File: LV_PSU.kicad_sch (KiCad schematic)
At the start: 25 parts, among them IC201 1769205241, J201 Header_Male_Pin_2.54mm_1X2_,_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, J202 PJ-082BH, U201 OKI-78SR-5_1.5-W36H-C, U202 AZ1117IH-3.3TRG1, U203 AZ1117IH-3.3TRG1

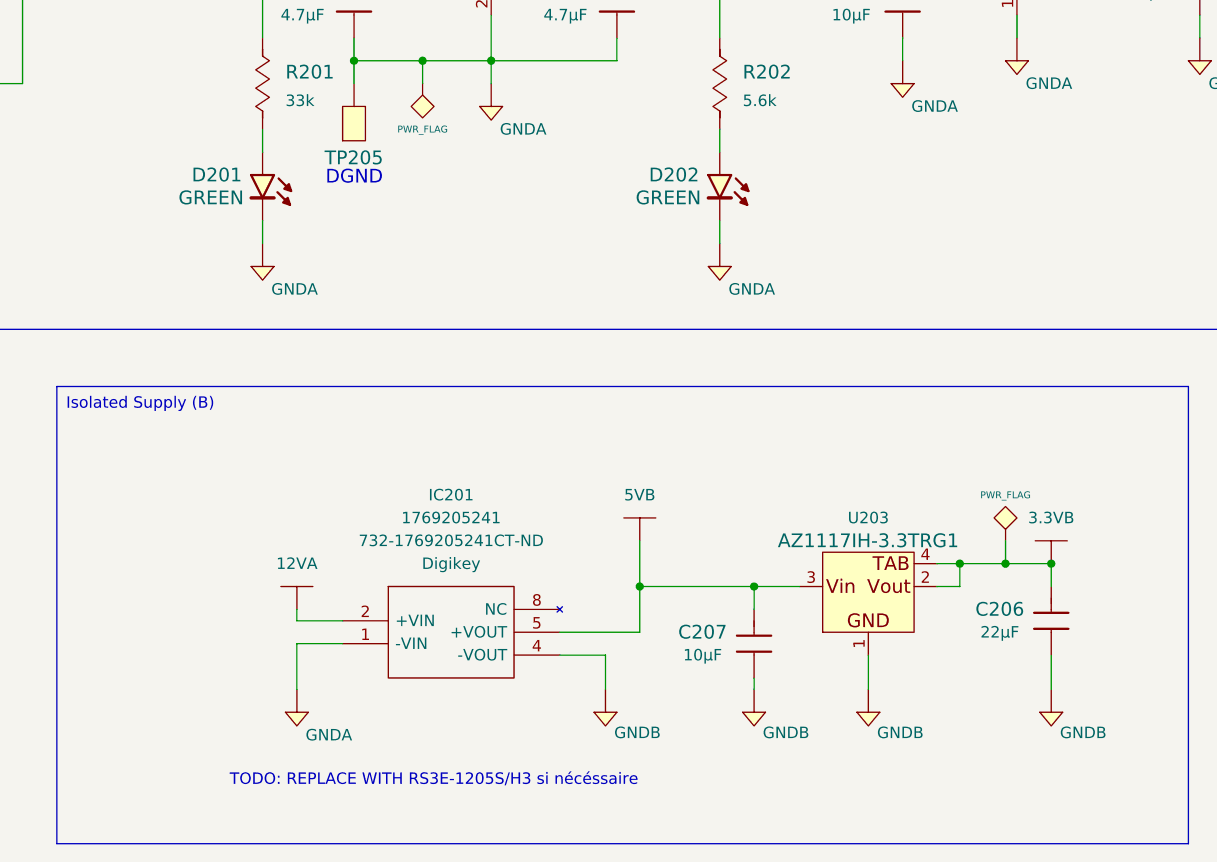
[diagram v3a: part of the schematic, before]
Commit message: update schematic
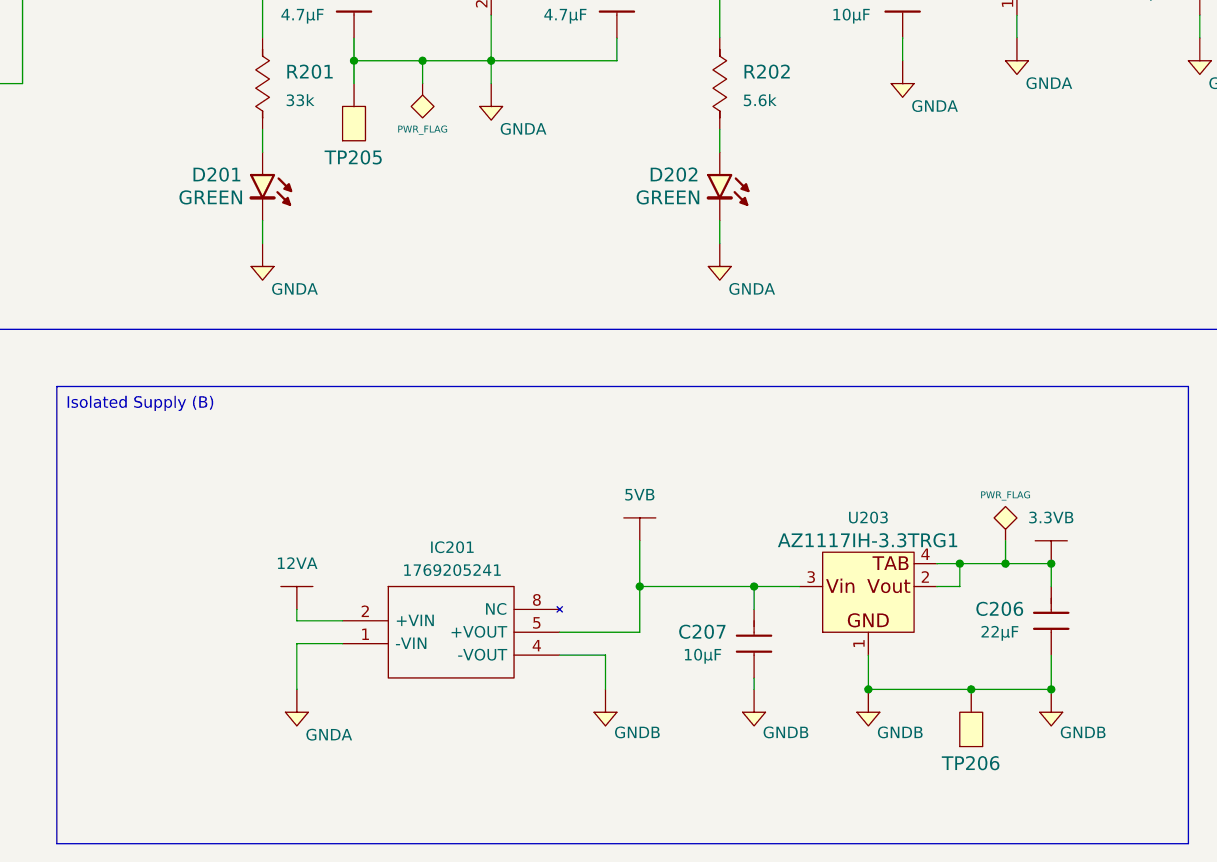
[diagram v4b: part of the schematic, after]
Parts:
- added TP206: Test_Point_THM, Connectors:Keystone_5001, symbol Connectors:Test_Point_THM
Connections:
- net GNDB: now also TP206.1 (TP)
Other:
- note removed: "DGND"
- note removed: "TODO: REPLACE WITH RS3E-1205S/H3 si nécéssaire"
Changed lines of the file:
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@@
 	)
 	(junction
+		(at 186.69 140.97)
+		(diameter 0)
+		(color 0 0 0 0)
+	)
+	(junction
 		(at 85.09 58.42)
 		(diameter 0)
@@
 	)
 	(junction
+		(at 175.26 140.97)
+		(diameter 0)
+		(color 0 0 0 0)
+	)
+	(junction
 		(at 118.11 71.12)
 		(diameter 0)
@@
 	)
 	(junction
+		(at 195.58 140.97)
+		(diameter 0)
+		(color 0 0 0 0)
+	)
+	(junction
 		(at 171.45 58.42)
 		(diameter 0)
@@
 	(wire
 		(pts
+			(xy 175.26 140.97) (xy 186.69 140.97)
+		)
+		(stroke
+			(width 0)
+			(type default)
+		)
+	)
+	(wire
+		(pts
 			(xy 185.42 127) (xy 185.42 129.54)
 		)
@@
 	(wire
 		(pts
+			(xy 186.69 140.97) (xy 195.58 140.97)
+		)
+		(stroke
+			(width 0)
+			(type default)
+		)
+	)
+	(wire
+		(pts
 			(xy 179.07 60.96) (xy 179.07 58.42)
 		)
@@
 		)
 	)
-	(text "TODO: REPLACE WITH RS3E-1205S/H3 si nécéssaire"
-		(exclude_from_sim no)
-		(at 127 151.13 0)
-		(effects
-			(font
-				(size 1.27 1.27)
-			)
-		)
-	)
 	(text "12V IN"
 		(exclude_from_sim no)
@@
 		)
 	)
-	(text "DGND"
-		(exclude_from_sim no)
-		(at 114.935 85.09 0)
-		(effects
-			(font
-				(size 1.524 1.524)
-			)
-			(justify left bottom)
-		)
-	)
 	(symbol
 		(lib_id "Connectors:PJ-082BH")
@@
 		(on_board yes)
 		(dnp no)
-		(fields_autoplaced yes)
 		(property "Reference" "IC201"
-			(at 128.905 119.38 0)
+			(at 129.032 125.222 0)
 			(effects
 				(font
@@
 		)
 		(property "Value" "1769205241"
-			(at 128.905 121.92 0)
+			(at 129.032 127.762 0)
 			(effects
 				(font
@@
 					(size 1.27 1.27)
 				)
+				(hide yes)
 			)
 		)
@@
 					(size 1.27 1.27)
 				)
+				(hide yes)
 			)
 		)
@@
 	)
 	(symbol
+		(lib_id "Connectors:Test_Point_THM")
+		(at 186.69 146.05 90)
+		(unit 1)
+		(exclude_from_sim no)
+		(in_bom yes)
+		(on_board yes)
+		(dnp no)
+		(property "Reference" "TP206"
+			(at 186.69 149.225 90)
+			(effects
+				(font
+					(size 1.524 1.524)
+				)
+			)
+		)
+		(property "Value" "Test_Point_THM"
+			(at 194.31 146.05 0)
+			(effects
+				(font
+					(size 1.524 1.524)
+				)
+				(hide yes)
+			)
+		)
+		(property "Footprint" "Connectors:Keystone_5001"
+			(at 209.55 146.05 0)
+			(effects
+				(font
+					(size 1.524 1.524)
+				)
+				(hide yes)
+			)
+		)
+		(property "Datasheet" "http://keyelco.com/userAssets/file/M65p56.pdf"
+			(at 212.09 146.05 0)
+			(effects
+				(font
+					(size 1.524 1.524)
+				)
+				(hide yes)
+			)
+		)
+		(property "Description" "TEST POINT PC MINI .040\"D BLACK"
+			(at 207.01 146.05 0)
+			(effects
+				(font
+					(size 1.524 1.524)
+				)
+				(hide yes)
+			)
+		)
+		(property "Supplier" "Digikey"
+			(at 196.85 146.05 0)
+			(effects
+				(font
+					(size 1.524 1.524)
+				)
+				(hide yes)
+			)
+		)
+		(property "Supplier Part Number" "36-5001-ND"
+			(at 199.39 146.05 0)
+			(effects
+				(font
+					(size 1.524 1.524)
+				)
+				(hide yes)
+			)
+		)
+		(property "Manufacturer" "Keystone Electronics"
+			(at 201.93 146.05 0)
+			(effects
+				(font
+					(size 1.524 1.524)
+				)
+				(hide yes)
+			)
+		)
+		(property "Manufacturer Part Number" "5001"
+			(at 204.47 146.05 0)
+			(effects
+				(font
+					(size 1.524 1.524)
+				)
+				(hide yes)
+			)
+		)
+		(pin "1"
+		)
+		(instances
+			(project "SACE-HW"
+				(path "/4c1e5ca8-aa0f-4a8e-bffe-6765adb2e3e8/0f8b1d52-3451-4d91-9a0f-fc5eea3d9449"
+					(reference "TP206")
+					(unit 1)
+				)
+			)
+		)
+	)
+	(symbol
 		(lib_id "Capacitors:885012107005")
 		(at 195.58 132.08 90)
@@
 		(on_board yes)
 		(dnp no)
-		(property "Reference" "#PWR0218"
+		(property "Reference" "#PWR0219"
 			(at 175.26 147.828 0)
 			(effects
@@
 			(project "SACE-HW"
 				(path "/4c1e5ca8-aa0f-4a8e-bffe-6765adb2e3e8/0f8b1d52-3451-4d91-9a0f-fc5eea3d9449"
-					(reference "#PWR0218")
+					(reference "#PWR0219")
 					(unit 1)
 				)
@@
 		(on_board yes)
 		(dnp no)
-		(property "Reference" "#PWR0219"
+		(property "Reference" "#PWR0220"
 			(at 195.58 147.828 0)
 			(effects
@@
 			(project "SACE-HW"
 				(path "/4c1e5ca8-aa0f-4a8e-bffe-6765adb2e3e8/0f8b1d52-3451-4d91-9a0f-fc5eea3d9449"
-					(reference "#PWR0219")
+					(reference "#PWR0220")
 					(unit 1)
 				)
@@
 		(on_board yes)
 		(dnp no)
-		(property "Reference" "#PWR0220"
+		(property "Reference" "#PWR0218"
 			(at 162.56 147.828 0)
 			(effects
@@
 			(project "SACE-HW"
 				(path "/4c1e5ca8-aa0f-4a8e-bffe-6765adb2e3e8/0f8b1d52-3451-4d91-9a0f-fc5eea3d9449"
-					(reference "#PWR0220")
+					(reference "#PWR0218")
 					(unit 1)
 				)

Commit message: modif schématique
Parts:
- removed C205, C207: 885012107014, Capacitors:C0805, symbol Capacitors:885012107014
- removed C206: 885012107005, Capacitors:C0805, symbol Capacitors:885012107005
- removed IC201: 1769205241, IC:1769205241, symbol PMIC:1769205241
- removed J201: Header_Male_Pin_2.54mm_1X2_,_Unshrouded, Connectors:Headers_2.54mm_1X2, symbol Connectors:Header_Male_Pin_2.54mm_1X2_,_Unshrouded
- removed J202: PJ-082BH, Connectors:CUI_PJ-082BH, symbol Connectors:PJ-082BH
- removed TP202: Test_Point_THM, Connectors:Keystone_5001, symbol Connectors:Test_Point_THM
- removed U203: AZ1117IH-3.3TRG1, IC:SOT-223-3, symbol PMIC:AZ1117IH-3.3TRG1
- added C205: 885012107005, Capacitors:C0805, symbol Capacitors:885012107005
- added C206, C207: 885012107018, Capacitors:C0805, symbol Capacitors:885012107018
- added C208: 885012107014, Capacitors:C0805, symbol Capacitors:885012107014
- added D204, D205, D206: 150080VS75000, Diodes:LED_0805_GREEN, symbol Diodes:150080VS75000
- added F202: 39511000440, Fuses:TE5_395, symbol Fuses:39511000440
- added J201, J203: 1935161, Connectors:1935161, symbol Connectors:1935161
- added J202: Header_Male_Pin_2.54mm_1X2_,_Unshrouded, Connectors:Headers_2.54mm_1X2, symbol Connectors:Header_Male_Pin_2.54mm_1X2_,_Unshrouded
- added R204: RC0805JR-0733KL, Resistors:R0805, symbol Resistors:RC0805JR-0733KL
- added R205: RC0805FR-075K6L, Resistors:R0805, symbol Resistors:RC0805FR-075K6L
- added R206: RC0805JR-072K2L, Resistors:R0805, symbol Resistors:RC0805JR-072K2L
- added TP205, TP207, TP208, TP209: Test_Point_THM, Connectors:Keystone_5001, symbol Connectors:Test_Point_THM
- added U203: OKI-78SR-5_1.5-W36H-C, Assembly:OKI-78SR_Horizontal, symbol PMIC:OKI-78SR-5_1.5-W36H-C
- added U204: AZ1117IH-3.3TRG1, IC:SOT-223-3, symbol PMIC:AZ1117IH-3.3TRG1
- renumbered TP203 to TP202, TP204 to TP203, TP205 to TP204
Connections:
- net 12VA: now also J201.2
- net 3.3VB: now also C205.2, J202.1, R206.2, TP205.1 (TP), U204.2 (Vout), U204.4 (Vout_(TAB))
- net 5VB: now also C207.2, C208.2, R205.2, TP208.1 (TP), U203.3 (Vout), U204.3 (Vin)
- net GNDA: now also J201.1
- net GNDB: now also C205.1, C206.1, C207.1, C208.1, D204.1 (Cathode), D205.1 (Cathode), D206.1 (Cathode), J203.1, TP209.1 (TP), U203.2 (GND), U204.1 (GND); no longer TP206.1 (TP)
- net VDD: now also TP206.1 (TP), J202.2
- new net: D205.2 (Anode), R205.1
- new net: C206.2, F202.2, R204.2, TP207.1 (TP), U203.1 (Vin)
- new net: D206.2 (Anode), R206.1
- new net: D204.2 (Anode), R204.1
- new net 12VB: F202.1, J203.2
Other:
- note removed: "3.3V (LDO)"
- note removed: "5V (SMPS)"
- moved on the sheet: C201, C202, C203, C204, D201, D202, D203, F201, R201, R202, R203, TP201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

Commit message: update schematique
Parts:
- renumbered C202 to C1, C206 to C2, C203 to C3, C207 to C4, C204 to C5, C208 to C6, C201 to C7, C205 to C8, D201 to D1, D204 to D2, D202 to D3, D205 to D4, D203 to D5, D206 to D6, F201 to F1, F202 to F2, J201 to J1, J203 to J2, J202 to J3, R201 to R1, R204 to R2, R202 to R3, R205 to R4, R203 to R5, R206 to R6, TP202 to TP1, TP207 to TP2, TP204 to TP3, TP209 to TP4, TP203 to TP5, TP208 to TP6, TP201 to TP7, TP205 to TP8, TP206 to TP9, U201 to U1, U203 to U2, U202 to U3, U204 to U4

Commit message: update schematique
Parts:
- removed C1, C3: 885012107018, Capacitors:C0805, symbol Capacitors:885012107018
- removed D1: 150080VS75000, Diodes:LED_0805_GREEN, symbol Diodes:150080VS75000
- removed F1: 39511000440, Fuses:TE5_395, symbol Fuses:39511000440
- removed J1: 1935161, Connectors:1935161, symbol Connectors:1935161
- removed R1: RC0805JR-0733KL, Resistors:R0805, symbol Resistors:RC0805JR-0733KL
- removed TP1, TP3: Test_Point_THM, Connectors:Keystone_5001, symbol Connectors:Test_Point_THM
- removed U1: OKI-78SR-5_1.5-W36H-C, Assembly:OKI-78SR_Horizontal, symbol PMIC:OKI-78SR-5_1.5-W36H-C
- added IC201: 1769205241, IC:1769205241, symbol PMIC:1769205241
- added J203: 2350514-8, Connectors:CONN8_2350514-8_TEC, symbol Connectors:2350514-8
- renumbered C7 to C201, C5 to C202, C8 to C203, C2 to C204, C4 to C205, C6 to C206, D3 to D201, D5 to D202, D2 to D203, D4 to D204, D6 to D205, F2 to F201, J3 to J201, J2 to J202, R3 to R201, R5 to R202, R2 to R203, R4 to R204, R6 to R205, TP7 to TP201, TP5 to TP202, TP8 to TP203, TP9 to TP204, TP2 to TP205, TP6 to TP206, TP4 to TP207, U3 to U201, U2 to U202, U4 to U203
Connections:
- net 12VB: now also IC201.2 (+VIN), J203.1, J203.2
- net 5VA: now also IC201.5 (+VOUT)
- net 5VB: now also J203.3, J203.4
- net GNDA: now also IC201.4 (-VOUT)
- net GNDB: now also IC201.1 (-VIN), J203.5, J203.6, J203.7, J203.8
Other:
- moved on the sheet: C201, C202, C203, C204, C205, C206, D201, D202, D203, D204, D205, F201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

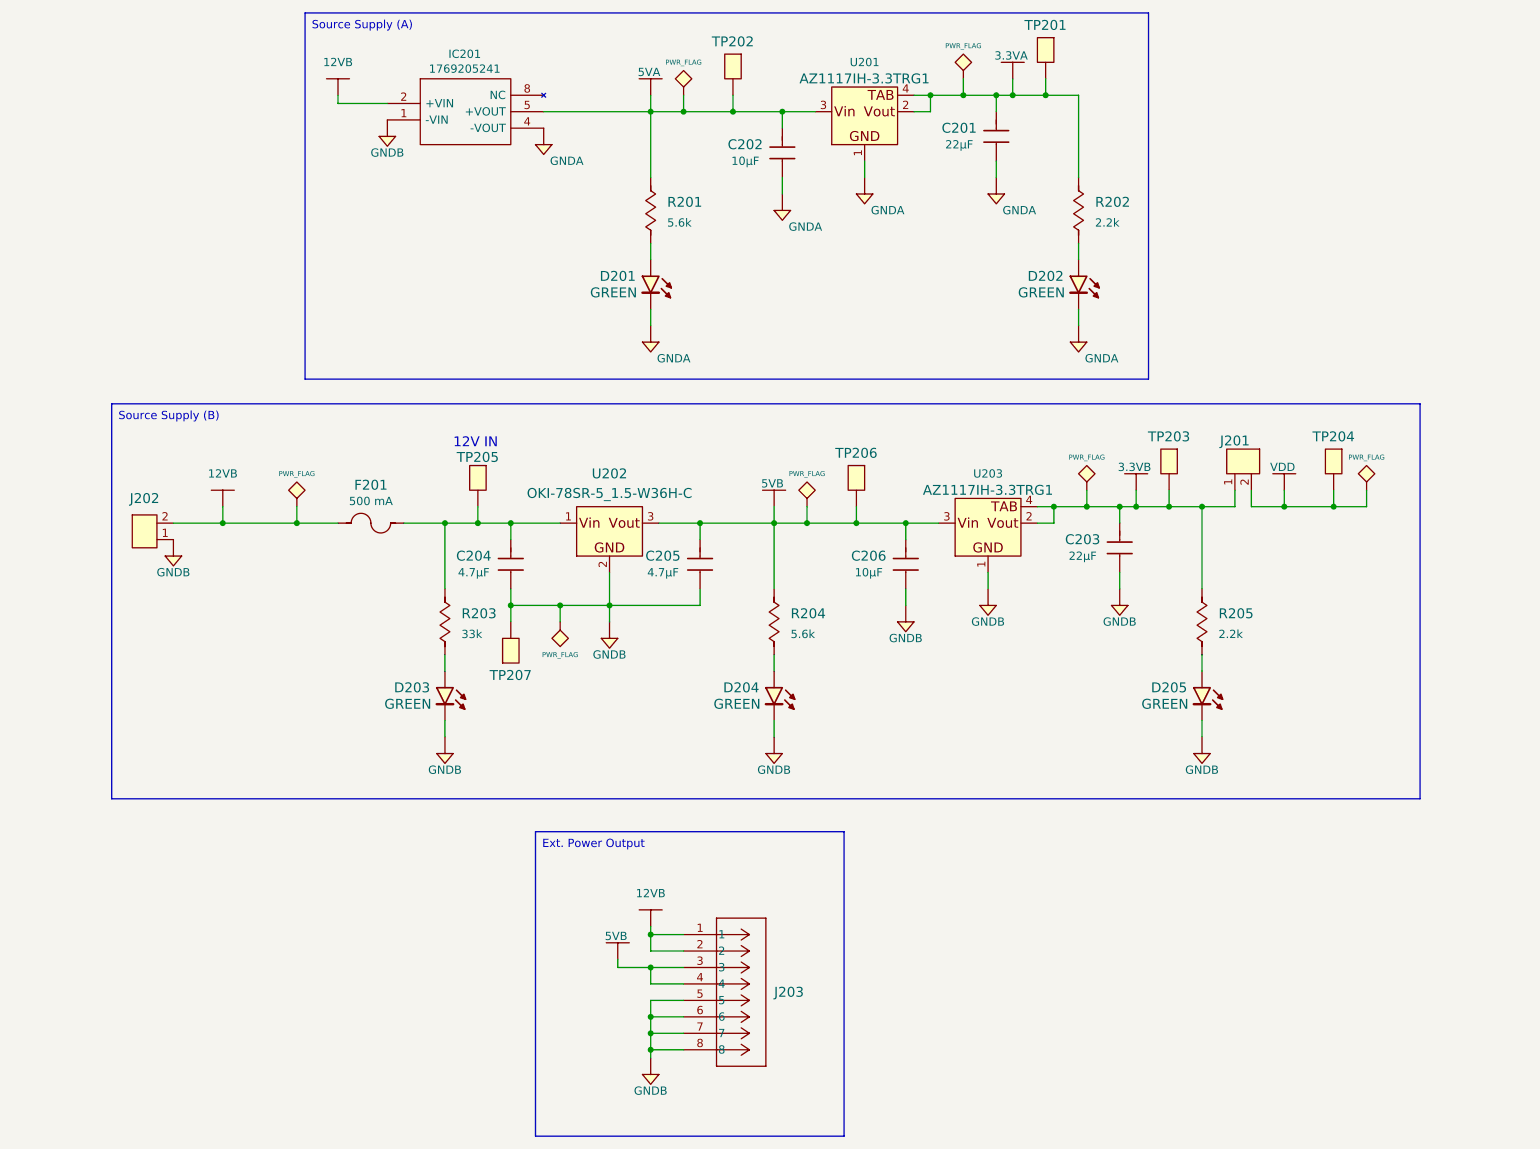
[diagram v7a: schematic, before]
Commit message: update schematic
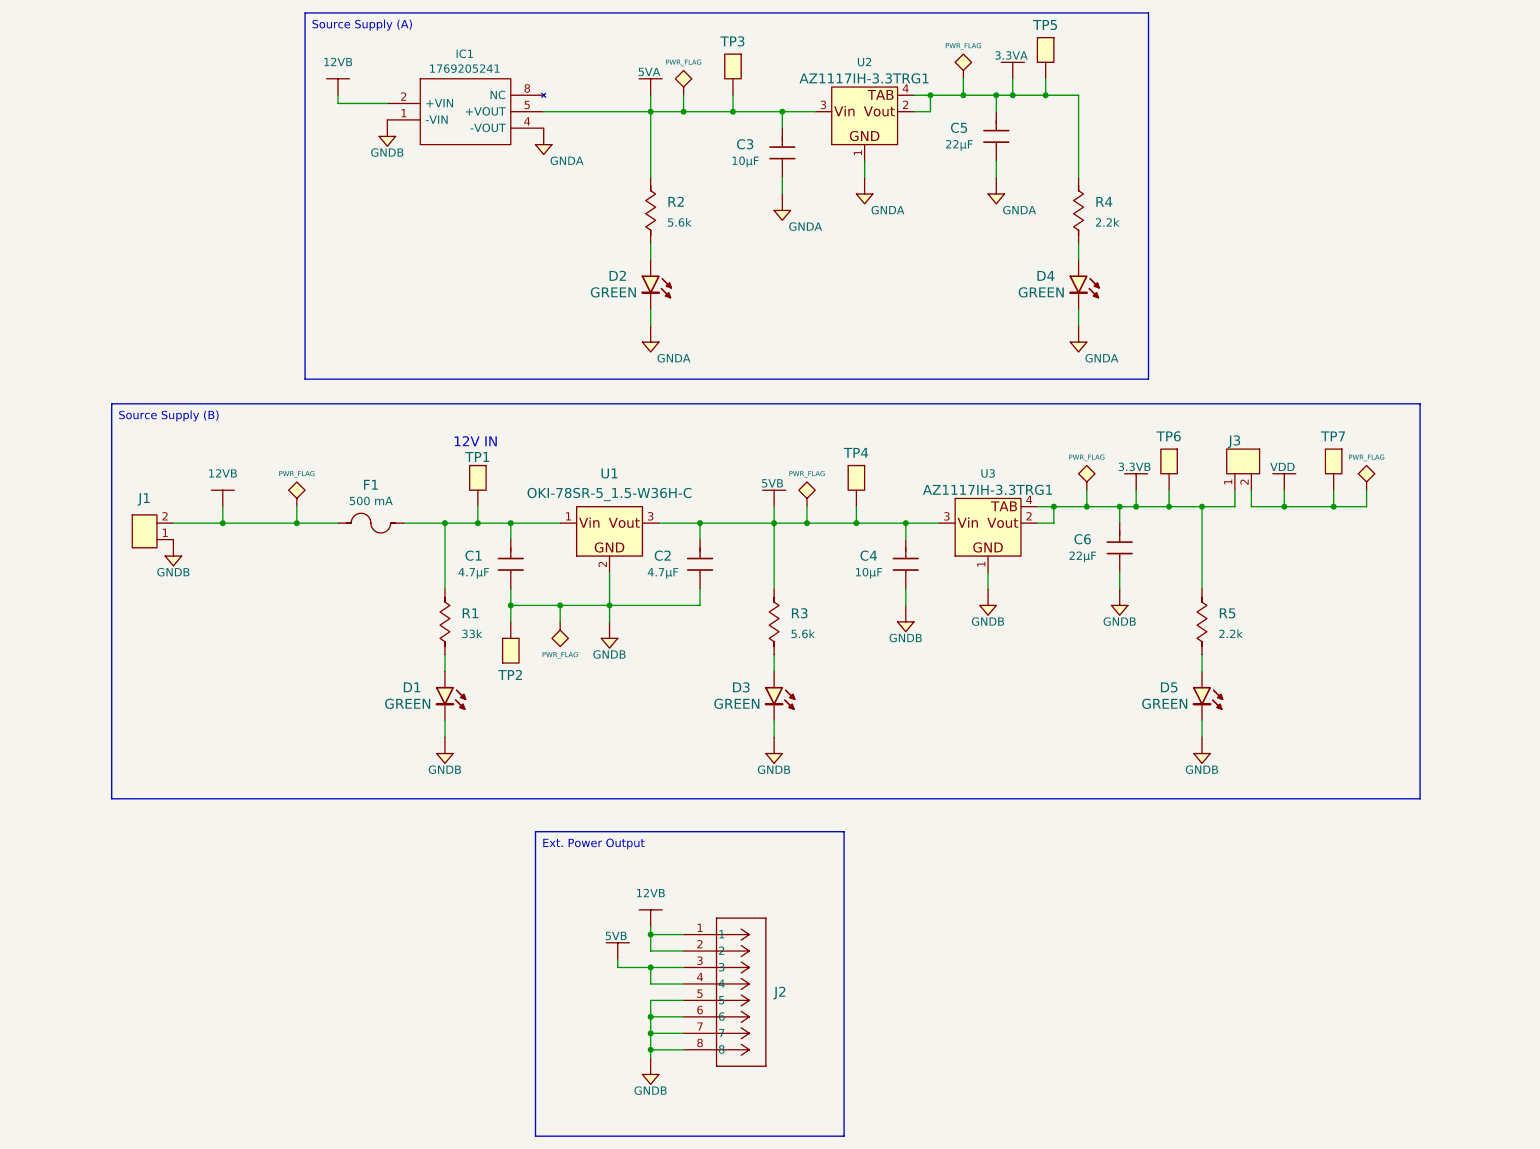
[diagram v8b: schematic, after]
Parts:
- renumbered C204 to C1, C205 to C2, C202 to C3, C206 to C4, C201 to C5, C203 to C6, D203 to D1, D201 to D2, D204 to D3, D202 to D4, D205 to D5, F201 to F1, IC201 to IC1, J202 to J1, J203 to J2, J201 to J3, R203 to R1, R201 to R2, R204 to R3, R202 to R4, R205 to R5, TP205 to TP1, TP207 to TP2, TP202 to TP3, TP206 to TP4, TP201 to TP5, TP203 to TP6, TP204 to TP7, U202 to U1, U201 to U2, U203 to U3
